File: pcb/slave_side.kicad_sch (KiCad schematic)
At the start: 2 parts, among them J6 AudioJack4

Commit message: feat: Add more components, add finalized outline
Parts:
- J6: footprint (none) -> Connector_Audio:Jack_3.5mm_CUI_SJ-3523-SMT_Horizontal
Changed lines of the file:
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@@
 			)
 		)
-		(property "Footprint" ""
+		(property "Footprint" "Connector_Audio:Jack_3.5mm_CUI_SJ-3523-SMT_Horizontal"
 			(at 46.99 60.96 0)
 			(effects

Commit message: feat: Further develop right side
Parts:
- removed J6: AudioJack4, Connector_Audio:Jack_3.5mm_CUI_SJ-3523-SMT_Horizontal, symbol Connector_Audio:AudioJack4
- added C18, C19: 10u, Capacitor_SMD:C_0805_2012Metric, symbol Device:C
- added D22, D23, D24, D25, D26, D27, D28, D29, D30, D31, D32, D33, D34, D35, D36, D37, D38, D39: D_Small, symbol Device:D_Small
- added D40: LED_Small, symbol Device:LED_Small
- added J4: 4P4C_Shielded, Connector_RJ:RJ9_Evercom_5301-440xxx_Horizontal, symbol Connector:4P4C_Shielded
- added R14: 10k, symbol library:R
- added SW20, SW21, SW22, SW23, SW24, SW25, SW26, SW27, SW28, SW29, SW30, SW31, SW32, SW33, SW34, SW35, SW36, SW37: SW_Push_45deg, ai03-MX_V2:MX-Solderable-1U, symbol Switch:SW_Push_45deg
- added TP8: TestPoint, TestPoint:TestPoint_Pad_D2.0mm, symbol Connector:TestPoint
- added U6: NCP1117LPST33T3G, NCP1117LPST33T3G:SOT230P700X175-4N, symbol NCP1117LPST33T3G:NCP1117LPST33T3G
- added U7: PCA9555DB, PCA9555DB_118:SOP65P775X200-24N, symbol Interface_Expansion:PCA9555DB
- added U8: PCA9956BTWY, PCA9956BTWY:SOP50P640X110-39N, symbol PCA9956BTWY:PCA9956BTWY
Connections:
- net +5V: now also D40.2 (A), U8.38 (VDD); no longer F3.2
- net at F3.1: now also J4.1
- new net: D24.1 (K), SW35.2
- new net: D37.1 (K), SW22.2
- new net: D32.1 (K), SW28.2
- new net: D27.1 (K), SW32.2
- new net: D34.1 (K), SW25.2
- new net: D40.1 (K), U8.6 (LED0)
- new net: D26.1 (K), SW33.2
- new net: D39.1 (K), SW20.2
- new net: D38.1 (K), SW21.2
- new net: D23.1 (K), SW36.2
- new net: D30.1 (K), SW30.2
- new net: D36.1 (K), SW23.2
- new net: D25.1 (K), SW34.2
- new net: D33.1 (K), SW27.2
- new net: D31.1 (K), SW29.2
- new net: R14.2, U7.1 (~{INT})
- new net: D28.1 (K), SW26.2
- new net: D35.1 (K), SW24.2
- new net: D22.1 (K), SW37.2
- new net: D29.1 (K), SW31.2
- new net +3V3_R: C19.1, TP8.1, U6.2 (OUTPUT), U6.4 (OUTPUT__1)
- new net +5V_R: C18.1, F3.2, R14.1, U6.3 (INPUT), U7.24 (VDD)
- new net COL1R: SW20.1, SW26.1, SW32.1, U7.7 (IO0_3)
- new net COL2R: SW21.1, SW27.1, SW33.1, U7.8 (IO0_4)
- new net COL3R: SW22.1, SW28.1, SW34.1, U7.9 (IO0_5)
- new net COL4R: SW23.1, SW29.1, SW35.1, U7.10 (IO0_6)
- new net COL5R: SW24.1, SW30.1, SW36.1, U7.11 (IO0_7)
- new net COL6R: SW25.1, SW31.1, SW37.1, U7.13 (IO1_0)
- new net GND_R: C18.2, C19.2, J4.2, J4.SH, U6.1 (GND), U7.12 (VSS), U7.2 (A1), U7.21 (A0), U7.3 (A2), U8.14 (VSS), U8.18 (VSS), U8.2 (AD0), U8.21 (VSS), U8.25 (VSS), U8.3 (AD1), U8.34 (VSS), U8.39 (EXP), U8.4 (AD2)
- new net ROW1R: D34.2 (A), D35.2 (A), D36.2 (A), D37.2 (A), D38.2 (A), D39.2 (A), U7.4 (IO0_0)
- new net ROW2R: D28.2 (A), D29.2 (A), D30.2 (A), D31.2 (A), D32.2 (A), D33.2 (A), U7.5 (IO0_1)
- new net ROW3R: D22.2 (A), D23.2 (A), D24.2 (A), D25.2 (A), D26.2 (A), D27.2 (A), U7.6 (IO0_2)
- new net S_M_CLOCK: J4.3, U7.22 (SCL), U8.36 (SCL)
- new net S_M_DATA: J4.4, U7.23 (SDA), U8.37 (SDA)
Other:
- note added: "EXP is the heatsink under the IC, make many thermal vias under the chip"
- note added: "I2C: 0000001"
- note added: "I2C: 0100000"
- note added: "how to route shield"
- note added: "same I2C adress as the LED driver on master side, but using different I2C bus, so no conflict"
- note removed: "I2C clock"
- note removed: "I2C data"

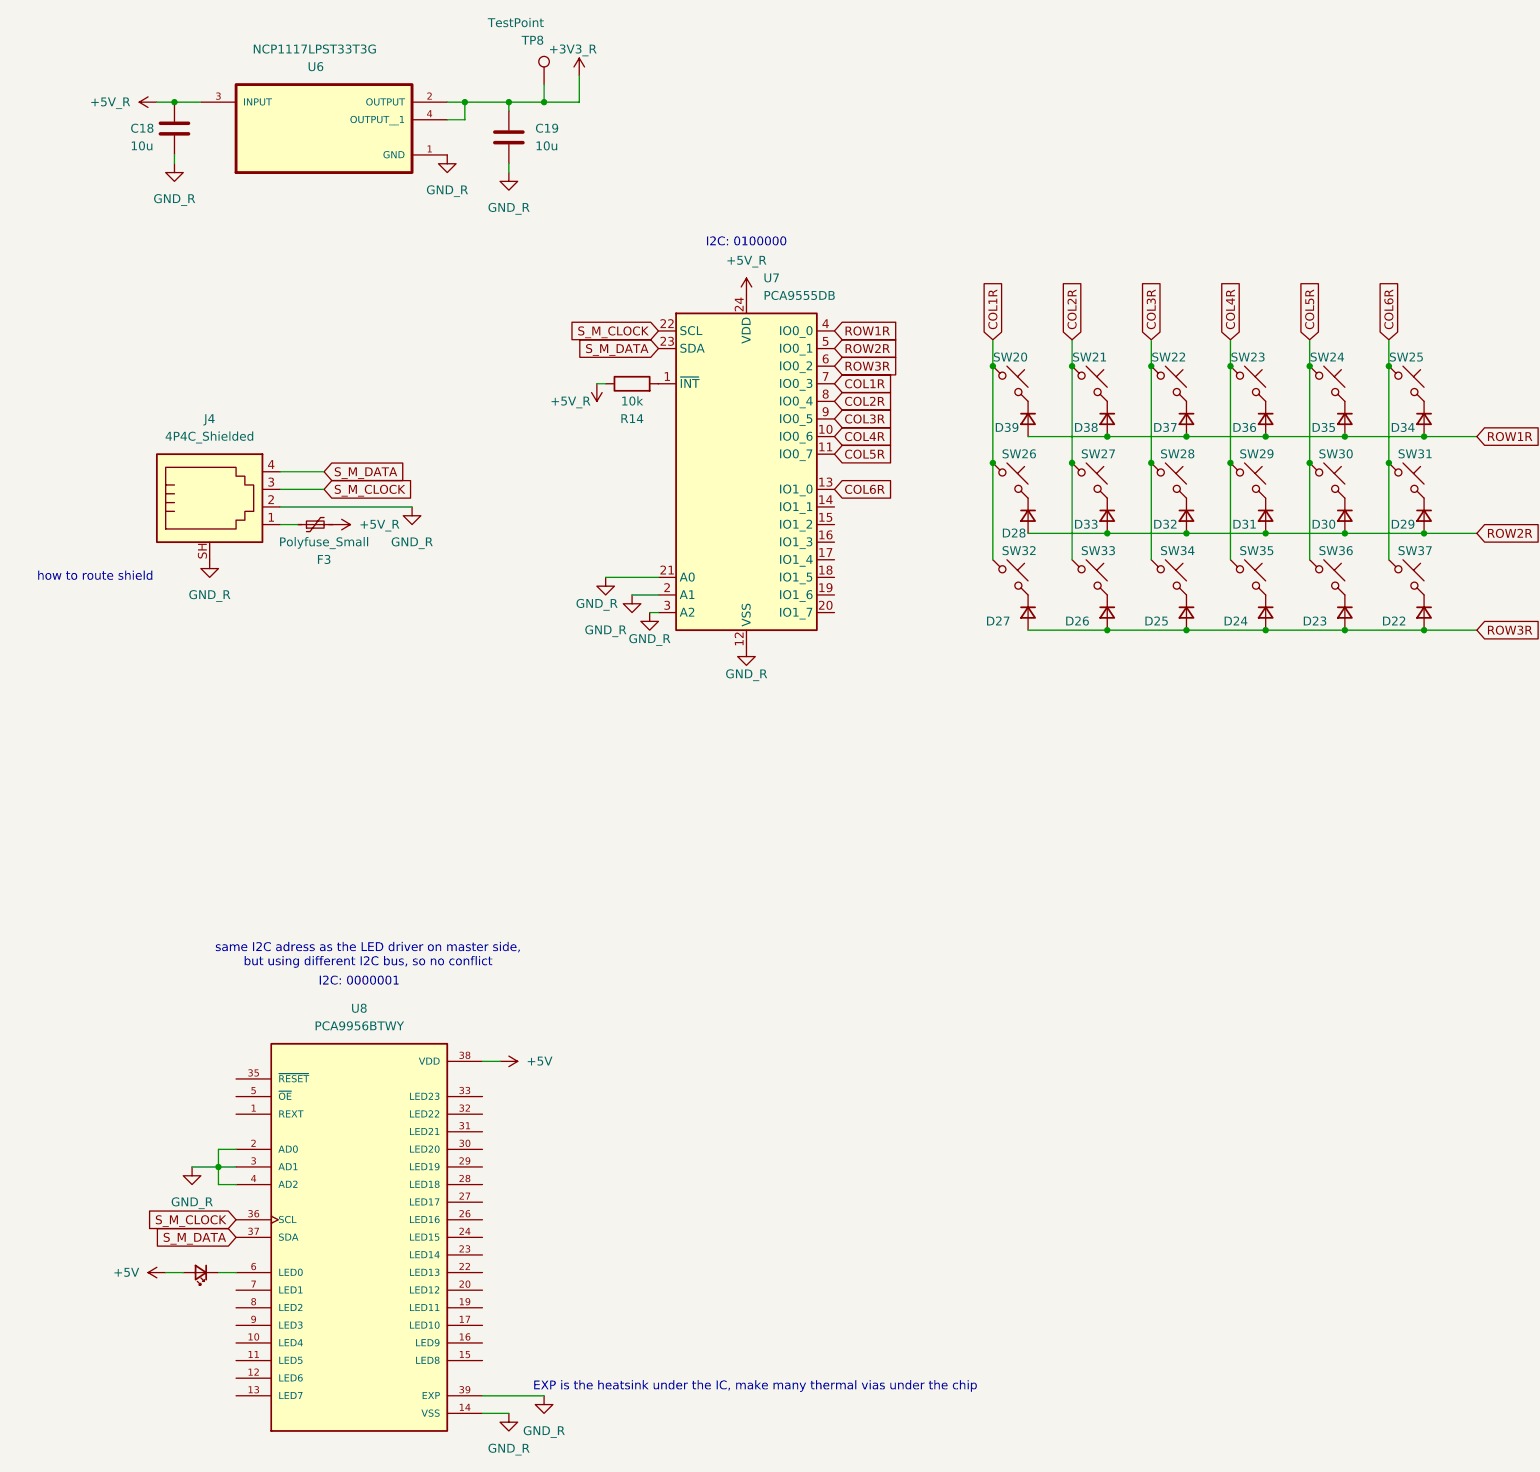
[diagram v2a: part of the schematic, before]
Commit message: fix: left/right nets separation
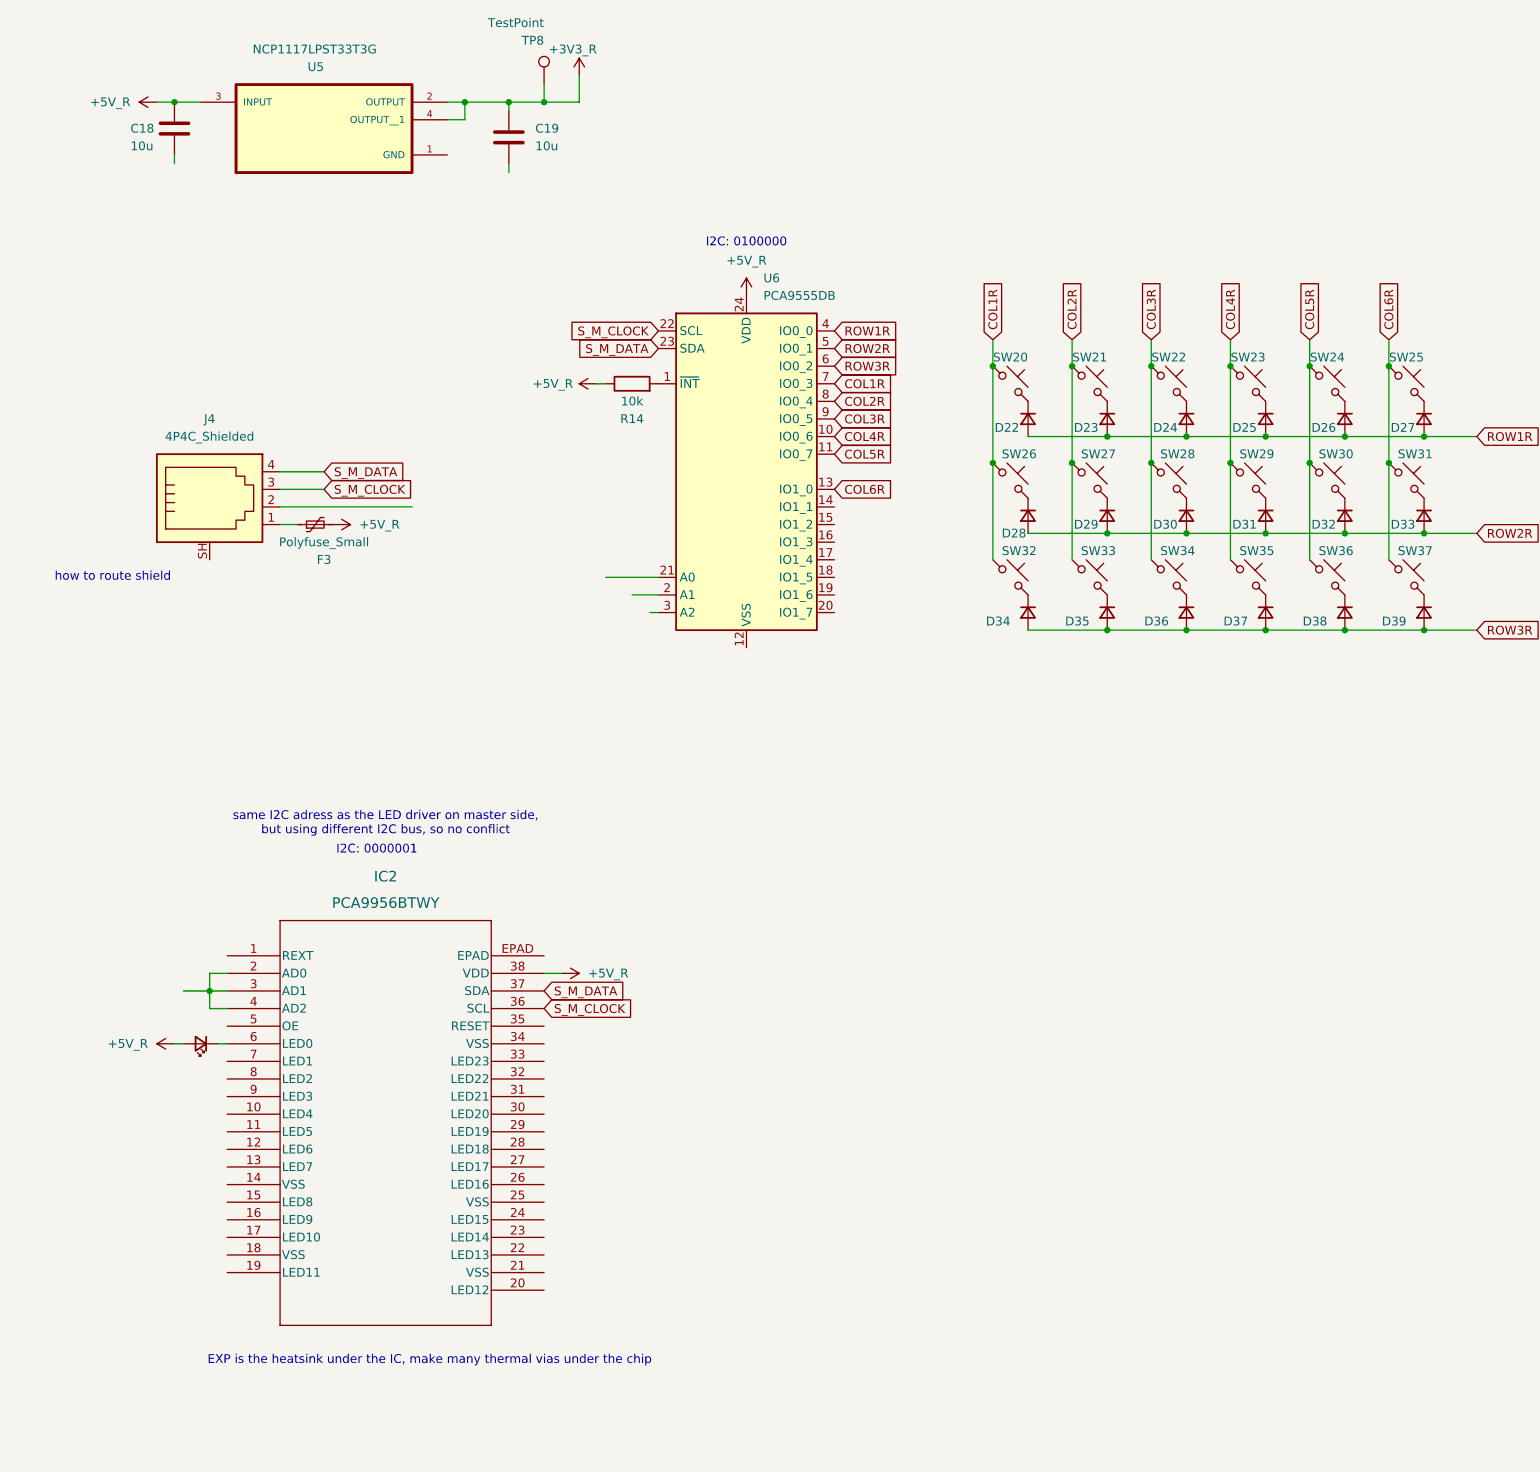
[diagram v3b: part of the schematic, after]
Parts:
- removed D40: LED_Small, symbol Device:LED_Small
- removed U8: PCA9956BTWY, PCA9956BTWY:SOP50P640X110-39N, symbol PCA9956BTWY:PCA9956BTWY
- added D41: LED_Small, symbol Device:LED_Small
- added IC2: PCA9956BTWY, HTSSOP38_4P4X9P7_NXP, symbol 2026-03-25_16-41-27:PCA9956BTWY
- renumbered D39 to D22, D38 to D23, D37 to D24, D36 to D25, D35 to D26, D34 to D27, D33 to D29, D32 to D30, D30 to D32, D29 to D33, D27 to D34, D26 to D35, D25 to D36, D24 to D37, D23 to D38, D22 to D39, U6 to U5, U7 to U6
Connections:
- net +5V_R: now also D41.2 (A), IC2.38 (VDD)
- net S_M_CLOCK: now also IC2.36 (SCL)
- net S_M_DATA: now also IC2.37 (SDA)
- removed net GND_R: C18.2, C19.2, J4.2, J4.SH, U5.1 (GND), U6.12 (VSS), U6.2 (A1), U6.21 (A0), U6.3 (A2)
- new net: IC2.2 (AD0), IC2.3 (AD1), IC2.4 (AD2)
- new net: D41.1 (K), IC2.6 (LED0)

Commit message: feat: Replace PCA9555 with MCP23017
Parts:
- removed U6: PCA9555DB, PCA9555DB_118:SOP65P775X200-24N, symbol Interface_Expansion:PCA9555DB
- added C18: 100n, Capacitor_SMD:C_0805_2012Metric, symbol library:C
- added C19: 20u, Capacitor_SMD:C_0805_2012Metric, symbol Device:C
- added D41, D42, D43, D44, D45, D46, D47, D48, D49, D50, D51, D52, D53, D54, D55, D56, D57, D58, D59, D60: LED_Small, symbol Device:LED_Small
- added R15, R16: 3.3k, Resistor_SMD:R_0402_1005Metric, symbol library:R
- added R17: 10k, Resistor_SMD:R_0402_1005Metric, symbol library:R
- added TP10, TP9: TestPoint, TestPoint:TestPoint_Pad_D2.0mm, symbol Connector:TestPoint
- added U7: OPT3001DNPR, OPT3001DNPR:SON65P200X200X65-7N, symbol OPT3001DNPR:OPT3001DNPR
- IC2: footprint HTSSOP38_4P4X9P7_NXP -> PCA9956BTWY:HTSSOP38_4P4X9P7_NXP
- R14: footprint (none) -> Resistor_SMD:R_0402_1005Metric
- renumbered C18 to C20, C19 to C21, D41 to D40
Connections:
- net +3V3_R: now also IC2.38 (VDD), R14.1, C18.1, R15.1, R16.1, U7.1 (VDD)
- net +5V_R: now also C19.1, D41.2 (A), D42.2 (A), D43.2 (A), D44.2 (A), D45.2 (A), D46.2 (A), D47.2 (A), D48.2 (A), D49.2 (A), D50.2 (A), D51.2 (A), D52.2 (A), D53.2 (A), D54.2 (A), D55.2 (A), D56.2 (A), D57.2 (A), D58.2 (A), D59.2 (A), D60.2 (A); no longer IC2.38 (VDD), R14.1
- net S_M_CLOCK: now also R16.2, U7.4 (SCL)
- net S_M_DATA: now also R15.2, U7.6 (SDA)
- net at IC2.10 (LED4): now also D44.1 (K)
- net at IC2.11 (LED5): now also D45.1 (K)
- net at IC2.12 (LED6): now also D46.1 (K)
- net at IC2.13 (LED7): now also D47.1 (K)
- net at IC2.15 (LED8): now also D48.1 (K)
- net at IC2.16 (LED9): now also D49.1 (K)
- net at IC2.17 (LED10): now also D50.1 (K)
- net at IC2.19 (LED11): now also D51.1 (K)
- net at IC2.20 (LED12): now also D52.1 (K)
- net at IC2.22 (LED13): now also D53.1 (K)
- net at IC2.23 (LED14): now also D54.1 (K)
- net at IC2.24 (LED15): now also D55.1 (K)
- net at IC2.26 (LED16): now also D56.1 (K)
- net at IC2.27 (LED17): now also D57.1 (K)
- net at IC2.28 (LED18): now also D58.1 (K)
- net at IC2.29 (LED19): now also D59.1 (K)
- net at IC2.30 (LED20): now also D60.1 (K)
- net at IC2.5 (OE): now also R17.2
- net at IC2.7 (LED1): now also D41.1 (K)
- net at IC2.8 (LED2): now also D42.1 (K)
- net at IC2.9 (LED3): now also D43.1 (K)
- net at R14.2: now also TP9.1
- new net: TP10.1, U7.5 (INT)
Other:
- note added: "I2C: 1000100"
- note added: "IO expander and kbd matrix"
- note added: "ambient light sensor"
- note added: "ensure pole rotation is correct (is the tab at the top or bottom), not flipped"
- note added: "exposed thermal pad"
- note added: "interrupt pin (unused, since polling from RP2040 over I2C)"
- note added: "thermal pad under IC"
- moved on the sheet: C20, C21, D22, D23, D24, D25, D26, D27, D28, D29, D30, D31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

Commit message: fix: I2C pullups on both buses
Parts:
- removed R15, R16: 3.3k, Resistor_SMD:R_0402_1005Metric, symbol library:R
- removed TP10: TestPoint, TestPoint:TestPoint_Pad_D2.0mm, symbol Connector:TestPoint
- added U5: MCP23017T-E/ML, MCP23017T_E_ML:QFN28_6x6MC_MCH, symbol 2026-03-26_18-01-23:MCP23017T-E_ML
- renumbered D60 to D45, D45 to D46, D59 to D47, D46 to D48, D58 to D49, D47 to D50, D57 to D51, D56 to D52, D48 to D53, D49 to D54, D50 to D56, D54 to D57, D53 to D58, D51 to D59, D52 to D60, R14 to R13, R17 to R14, TP8 to TP7, TP9 to TP8, U5 to U6
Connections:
- net +3V3_R: now also U5.5 (VDD)
- net COL1R: now also U5.20 (GPA3)
- net COL2R: now also U5.21 (GPA4)
- net COL3R: now also U5.22 (GPA5)
- net COL4R: now also U5.23 (GPA6)
- net COL5R: now also U5.24 (GPA7)
- net COL6R: now also U5.25 (GPB0)
- net ROW1R: now also U5.17 (GPA0)
- net ROW2R: now also U5.18 (GPA1)
- net ROW3R: now also U5.19 (GPA2)
- net S_M_CLOCK: now also U5.8 (SCL)
- net S_M_DATA: now also U5.9 (SDA)
- new net: U5.11 (A0), U5.12 (A1), U5.13 (A2)
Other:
- note added: "NC = not connected"
- moved on the sheet: R13, TP8
